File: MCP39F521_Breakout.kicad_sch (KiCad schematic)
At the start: 32 parts, among them J1 TEST_1P, J10 Conn_01x01, J11 Conn_01x10, J2 Conn_01x01, J3 Conn_01x01, J4 Conn_01x01, J5 Conn_01x01, J6 TEST_1P, J7 TEST_1P, J8 Conn_01x01, J9 Conn_01x01, U1 MCP39F521

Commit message: More wiring
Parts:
- added R11, R12: 2.4R, Resistor_SMD:R_0603_1608Metric, symbol Device:R
- J11: DNP (none) -> ...
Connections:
- net +3V3: now also J11.1 (Pin_1)
- net GNDA: now also R11.2, R12.1
- net GNDD: now also J11.10 (Pin_10)
- net SDA: now reaches R10.2, U1.14 (SDA)
- net SDA: now also J11.7 (Pin_7)
- net VP: now reaches J11.2 (Pin_2)
- net VP: now also C2.2, R2.2, U1.19 (V1+)
- net VN: now reaches J11.3 (Pin_3)
- net VN: now also C1.1, R1.1, U1.18 (V1-)
- net ~RESET: now reaches J11.4 (Pin_4)
- net ~RESET: now also R5.2, U1.10 (RESET\)
- net PWM: now reaches J11.5 (Pin_5)
- net SCL: now reaches J11.6 (Pin_6)
- net SCL: now also R9.2, U1.13 (SCL)
- net IP: now reaches J11.8 (Pin_8)
- net IP: now also L1.2, R12.2
- net IN: now reaches J11.9 (Pin_9)
- net IN: now also L2.2, R11.1

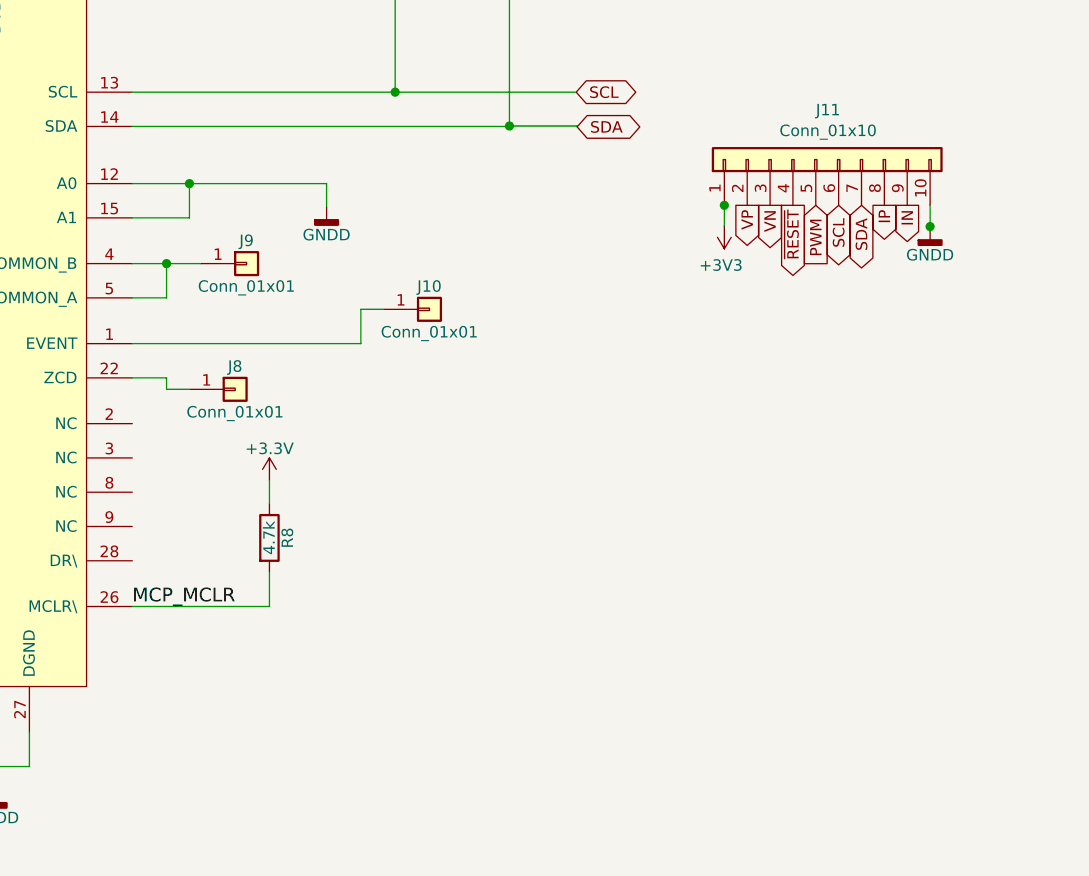
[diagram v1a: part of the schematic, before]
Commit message: Add address jumpers
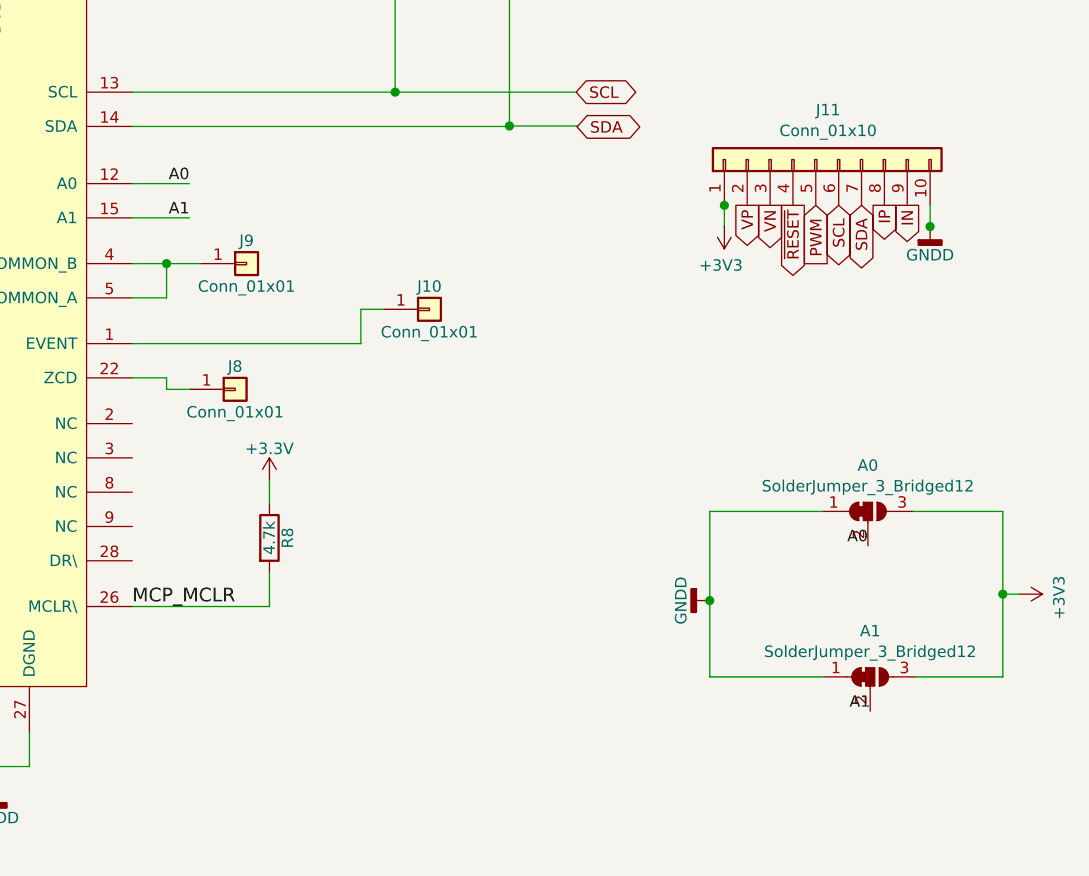
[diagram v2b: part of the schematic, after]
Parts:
- added A0, A1: SolderJumper_3_Bridged12, Jumper:SolderJumper-3_P1.3mm_Bridged12_Pad1.0x1.5mm, symbol Jumper:SolderJumper_3_Bridged12
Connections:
- net +3V3: now also A0.3 (B), A1.3 (B)
- net GNDD: now also A0.1 (A), A1.1 (A); no longer U1.12 (A0), U1.15 (A1)
- new net A0: A0.2 (C), U1.12 (A0)
- new net A1: A1.2 (C), U1.15 (A1)
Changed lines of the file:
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@@
   (junction (at 172.8724 111.76) (diameter 1.016) (color 0 0 0 0))
   (junction (at 174.1424 54.61) (diameter 1.016) (color 0 0 0 0))
-  (junction (at 175.4124 102.87) (diameter 1.016) (color 0 0 0 0))
   (junction (at 198.2724 54.61) (diameter 1.016) (color 0 0 0 0))
   (junction (at 198.2724 92.71) (diameter 1.016) (color 0 0 0 0))
   (junction (at 210.9724 54.61) (diameter 1.016) (color 0 0 0 0))
   (junction (at 210.9724 96.4692) (diameter 1.016) (color 0 0 0 0))
+  (junction (at 233.2228 149.1996) (diameter 1.016) (color 0 0 0 0))
   (junction (at 234.8484 105.283) (diameter 1.016) (color 0 0 0 0))
   (junction (at 257.7084 107.6452) (diameter 1.016) (color 0 0 0 0))
+  (junction (at 265.7856 148.4884) (diameter 1.016) (color 0 0 0 0))
   (wire (pts (xy 62.3824 163.83) (xy 76.3524 163.83))
     (stroke (width 0) (type solid) (color 0 0 0 0))
@@
     (stroke (width 0) (type solid) (color 0 0 0 0))
   )
-  (wire (pts (xy 175.4124 102.87) (xy 190.6524 102.87))
-    (stroke (width 0) (type solid) (color 0 0 0 0))
-  )
-  (wire (pts (xy 175.4124 106.68) (xy 175.4124 102.87))
-    (stroke (width 0) (type solid) (color 0 0 0 0))
-  )
   (wire (pts (xy 175.4124 125.73) (xy 172.8724 125.73))
     (stroke (width 0) (type solid) (color 0 0 0 0))
@@
     (stroke (width 0) (type solid) (color 0 0 0 0))
   )
-  (wire (pts (xy 190.6524 102.87) (xy 190.6524 105.41))
-    (stroke (width 0) (type solid) (color 0 0 0 0))
-  )
   (wire (pts (xy 194.4624 116.84) (xy 194.4624 120.65))
     (stroke (width 0) (type solid) (color 0 0 0 0))
@@
     (stroke (width 0) (type solid) (color 0 0 0 0))
   )
+  (wire (pts (xy 233.2228 139.2936) (xy 245.7196 139.2936))
+    (stroke (width 0) (type solid) (color 0 0 0 0))
+  )
+  (wire (pts (xy 233.2228 149.1996) (xy 233.2228 139.2936))
+    (stroke (width 0) (type solid) (color 0 0 0 0))
+  )
+  (wire (pts (xy 233.2228 157.6832) (xy 233.2228 149.1996))
+    (stroke (width 0) (type solid) (color 0 0 0 0))
+  )
   (wire (pts (xy 234.8484 105.156) (xy 234.8484 105.283))
     (stroke (width 0) (type solid) (color 0 0 0 0))
@@
     (stroke (width 0) (type solid) (color 0 0 0 0))
   )
+  (wire (pts (xy 245.9736 157.6832) (xy 233.2228 157.6832))
+    (stroke (width 0) (type solid) (color 0 0 0 0))
+  )
+  (wire (pts (xy 255.8796 139.2936) (xy 265.7856 139.2936))
+    (stroke (width 0) (type solid) (color 0 0 0 0))
+  )
   (wire (pts (xy 257.7084 105.283) (xy 257.7084 107.6452))
     (stroke (width 0) (type solid) (color 0 0 0 0))
   )
   (wire (pts (xy 257.7084 107.6452) (xy 257.7084 107.696))
+    (stroke (width 0) (type solid) (color 0 0 0 0))
+  )
+  (wire (pts (xy 265.7856 139.2936) (xy 265.7856 148.4884))
+    (stroke (width 0) (type solid) (color 0 0 0 0))
+  )
+  (wire (pts (xy 265.7856 148.4884) (xy 265.7856 157.6832))
+    (stroke (width 0) (type solid) (color 0 0 0 0))
+  )
+  (wire (pts (xy 265.7856 148.4884) (xy 267.6652 148.4884))
+    (stroke (width 0) (type solid) (color 0 0 0 0))
+  )
+  (wire (pts (xy 265.7856 157.6832) (xy 256.1336 157.6832))
     (stroke (width 0) (type solid) (color 0 0 0 0))
   )
   (label "MCP_MCLR" (at 169.0624 149.86 0)
     (effects (font (size 1.524 1.524)) (justify left bottom))
+  )
+  (label "A0" (at 175.4124 102.87 180)
+    (effects (font (size 1.27 1.27)) (justify right bottom))
+  )
+  (label "A1" (at 175.4124 106.68 180)
+    (effects (font (size 1.27 1.27)) (justify right bottom))
+  )
+  (label "A0" (at 250.7996 143.1036 180)
+    (effects (font (size 1.27 1.27)) (justify right bottom))
+  )
+  (label "A1" (at 251.0536 161.4932 180)
+    (effects (font (size 1.27 1.27)) (justify right bottom))
   )
   (global_label "VN" (shape input) (at 62.3824 163.83 180)    (property "Intersheet References" "${INTERSHEET_REFS}" (id 0) (at 56.0263 163.7506 0)
@@
     )
   )
+  (symbol (lib_id "power:+3V3") (at 267.6652 148.4884 270) (unit 1)
+    (in_bom yes) (on_board yes)
+    (property "Reference" "#PWR?" (id 0) (at 263.8552 148.4884 0)
+      (effects (font (size 1.27 1.27)) hide)
+    )
+    (property "Value" "+3V3" (id 1) (at 272.0594 148.8694 0))
+    (property "Footprint" "" (id 2) (at 267.6652 148.4884 0)
+      (effects (font (size 1.27 1.27)) hide)
+    )
+    (property "Datasheet" "" (id 3) (at 267.6652 148.4884 0)
+      (effects (font (size 1.27 1.27)) hide)
+    )
+  )
   (symbol (lib_id "power:GNDD") (at 153.8224 41.91 0) (unit 1)
     (in_bom yes) (on_board yes)
@@
     )
   )
-  (symbol (lib_id "power:GNDD") (at 190.6524 105.41 0) (unit 1)
-    (in_bom yes) (on_board yes)
-    (property "Reference" "#PWR0106" (id 0) (at 190.6524 111.76 0)
-      (effects (font (size 1.27 1.27)) hide)
-    )
-    (property "Value" "GNDD" (id 1) (at 190.6524 108.585 0))
-    (property "Footprint" "" (id 2) (at 190.6524 105.41 0)
-      (effects (font (size 1.27 1.27)) hide)
-    )
-    (property "Datasheet" "" (id 3) (at 190.6524 105.41 0)
+  (symbol (lib_id "power:GNDD") (at 233.2228 149.1996 270) (unit 1)
+    (in_bom yes) (on_board yes)
+    (property "Reference" "#PWR0106" (id 0) (at 226.8728 149.1996 0)
+      (effects (font (size 1.27 1.27)) hide)
+    )
+    (property "Value" "GNDD" (id 1) (at 230.0478 149.1996 0))
+    (property "Footprint" "" (id 2) (at 233.2228 149.1996 0)
+      (effects (font (size 1.27 1.27)) hide)
+    )
+    (property "Datasheet" "" (id 3) (at 233.2228 149.1996 0)
       (effects (font (size 1.27 1.27)) hide)
     )
@@
     )
   )
+  (symbol (lib_id "Jumper:SolderJumper_3_Bridged12") (at 250.7996 139.2936 0) (unit 1)
+    (in_bom yes) (on_board yes)
+    (property "Reference" "A0" (id 0) (at 250.8 134.1942 0))
+    (property "Value" "SolderJumper_3_Bridged12" (id 1) (at 250.7996 136.4931 0))
+    (property "Footprint" "Jumper:SolderJumper-3_P1.3mm_Bridged12_Pad1.0x1.5mm" (id 2) (at 250.7996 139.2936 0)
+      (effects (font (size 1.27 1.27)) hide)
+    )
+    (property "Datasheet" "~" (id 3) (at 250.7996 139.2936 0)
+      (effects (font (size 1.27 1.27)) hide)
+    )
+  )
+  (symbol (lib_id "Jumper:SolderJumper_3_Bridged12") (at 251.0536 157.6832 0) (unit 1)
+    (in_bom yes) (on_board yes)
+    (property "Reference" "A1" (id 0) (at 251.054 152.5844 0))
+    (property "Value" "SolderJumper_3_Bridged12" (id 1) (at 251.0536 154.8827 0))
+    (property "Footprint" "Jumper:SolderJumper-3_P1.3mm_Bridged12_Pad1.0x1.5mm" (id 2) (at 251.0536 157.6832 0)
+      (effects (font (size 1.27 1.27)) hide)
+    )
+    (property "Datasheet" "~" (id 3) (at 251.0536 157.6832 0)
+      (effects (font (size 1.27 1.27)) hide)
+    )
+  )
   (symbol (lib_id "Connector_Generic:Conn_01x10") (at 245.0084 100.203 90) (unit 1)
     (in_bom yes) (on_board yes)
@@
       (reference "#PWR0118") (unit 1) (value "GNDA") (footprint "")
     )
+    (path "/f698ad41-2dde-41c2-8138-e966600dc1e9"
+      (reference "#PWR?") (unit 1) (value "+3V3") (footprint "")
+    )
+    (path "/248b232d-dcba-4eaf-b58a-7bd31f6c6882"
+      (reference "A0") (unit 1) (value "SolderJumper_3_Bridged12") (footprint "Jumper:SolderJumper-3_P1.3mm_Bridged12_Pad1.0x1.5mm")
+    )
+    (path "/53766990-f259-4f3f-9026-616b13c50c35"
+      (reference "A1") (unit 1) (value "SolderJumper_3_Bridged12") (footprint "Jumper:SolderJumper-3_P1.3mm_Bridged12_Pad1.0x1.5mm")
+    )
     (path "/ee66d4e3-7ed2-42cc-96ea-fdce85276bc4"

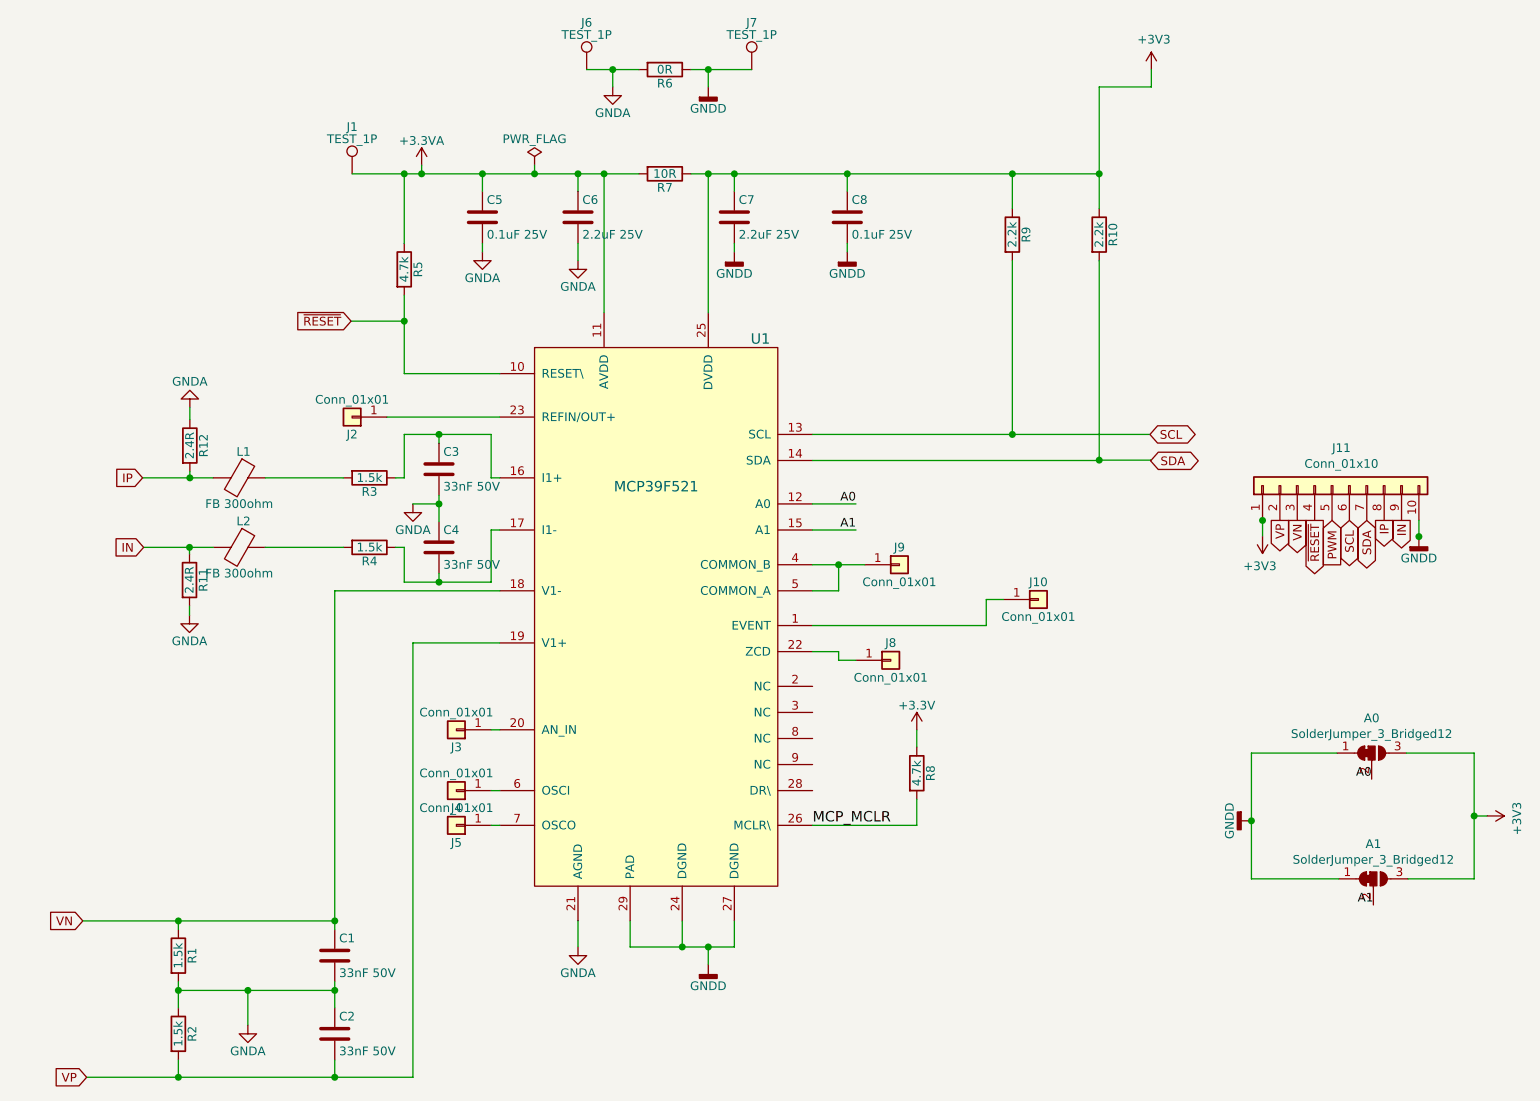
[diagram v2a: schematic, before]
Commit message: Cleanup copy-pasted symbols and perform initial autoroute
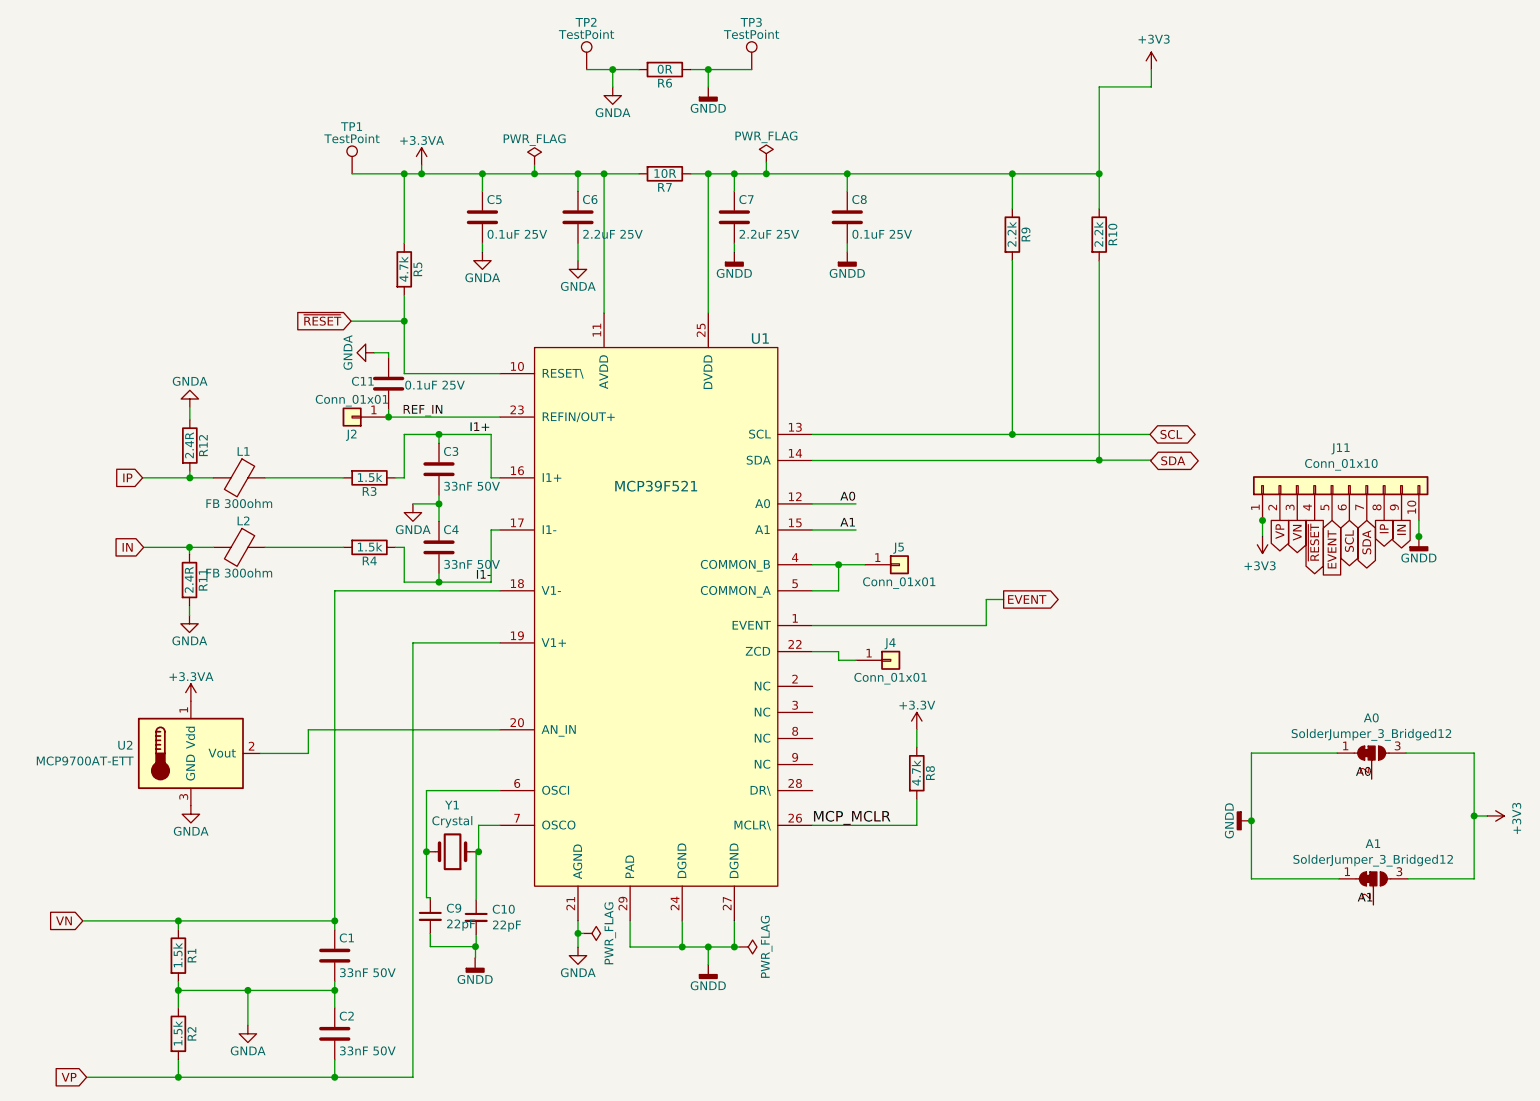
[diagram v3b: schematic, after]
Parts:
- removed J10, J3, J4, J5: Conn_01x01, TestPoint:TestPoint_Pad_1.5x1.5mm, symbol PowerMonitor-rescue:Conn_01x01
- added C10, C9: 22pF, Capacitor_SMD:C_0603_1608Metric, symbol Device:C_Small
- added C11: 0.1uF 25V, Capacitor_SMD:C_0603_1608Metric, symbol Device:C
- added U2: MCP9700AT-ETT, Package_TO_SOT_SMD:SOT-23, symbol Sensor_Temperature:MCP9700AT-ETT
- added Y1: Crystal, Crystal:Crystal_SMD_HC49-SD, symbol Device:Crystal
- C1, C2, C3, C4: footprint Capacitor_SMD:C_0805_2012Metric -> Capacitor_SMD:C_0603_1608Metric
- J2: symbol PowerMonitor-rescue:Conn_01x01 -> Connector_Generic:Conn_01x01
- J4: renamed from J8; symbol PowerMonitor-rescue:Conn_01x01 -> Connector_Generic:Conn_01x01
- J5: renamed from J9; symbol PowerMonitor-rescue:Conn_01x01 -> Connector_Generic:Conn_01x01
- L1, L2: footprint Inductor_SMD:L_0805_2012Metric -> Inductor_SMD:L_0603_1608Metric
- R1, R2, R3, R4, R7: footprint Resistor_SMD:R_0805_2012Metric -> Resistor_SMD:R_0603_1608Metric
- TP1: renamed from J1; value TEST_1P -> TestPoint; symbol PowerMonitor-rescue:TEST_1P -> Connector:TestPoint
- TP2: renamed from J6; value TEST_1P -> TestPoint; symbol PowerMonitor-rescue:TEST_1P -> Connector:TestPoint
- TP3: renamed from J7; value TEST_1P -> TestPoint; symbol PowerMonitor-rescue:TEST_1P -> Connector:TestPoint
- U1: symbol PowerMonitor-rescue:MCP39F521 -> mcp39f521:MCP39F521
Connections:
- net PWM is gone; now on net EVENT: J11.5 (Pin_5)
- net +3.3VA: now also U2.1 (Vdd)
- net GNDA: now also C11.1, U2.3 (GND)
- net GNDD: now also C10.2, C9.2
- net EVENT: now reaches U1.1 (EVENT)
- net I1-: now reaches C4.2, R4.1, U1.17 (I1-)
- net at U1.6 (OSCI): now also C9.1, Y1.2
- net I1+: now reaches C3.1, R3.1, U1.16 (I1+)
- net REF_IN: now reaches J2.1 (Pin_1), U1.23 (REFIN/OUT+)
- net REF_IN: now also C11.2
- net at U1.7 (OSCO): now also C10.1, Y1.1
- net at U1.20 (AN_IN): now also U2.2 (Vout)
